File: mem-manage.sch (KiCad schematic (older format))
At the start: 15 parts, among them J2 Close to enable CAS latch, J3 Close to enable CAS latch, U11 8721, U3 74LS138, U31 74LS00, U54 74LS32, U61 74LS08, U7 8722, U9 74F32

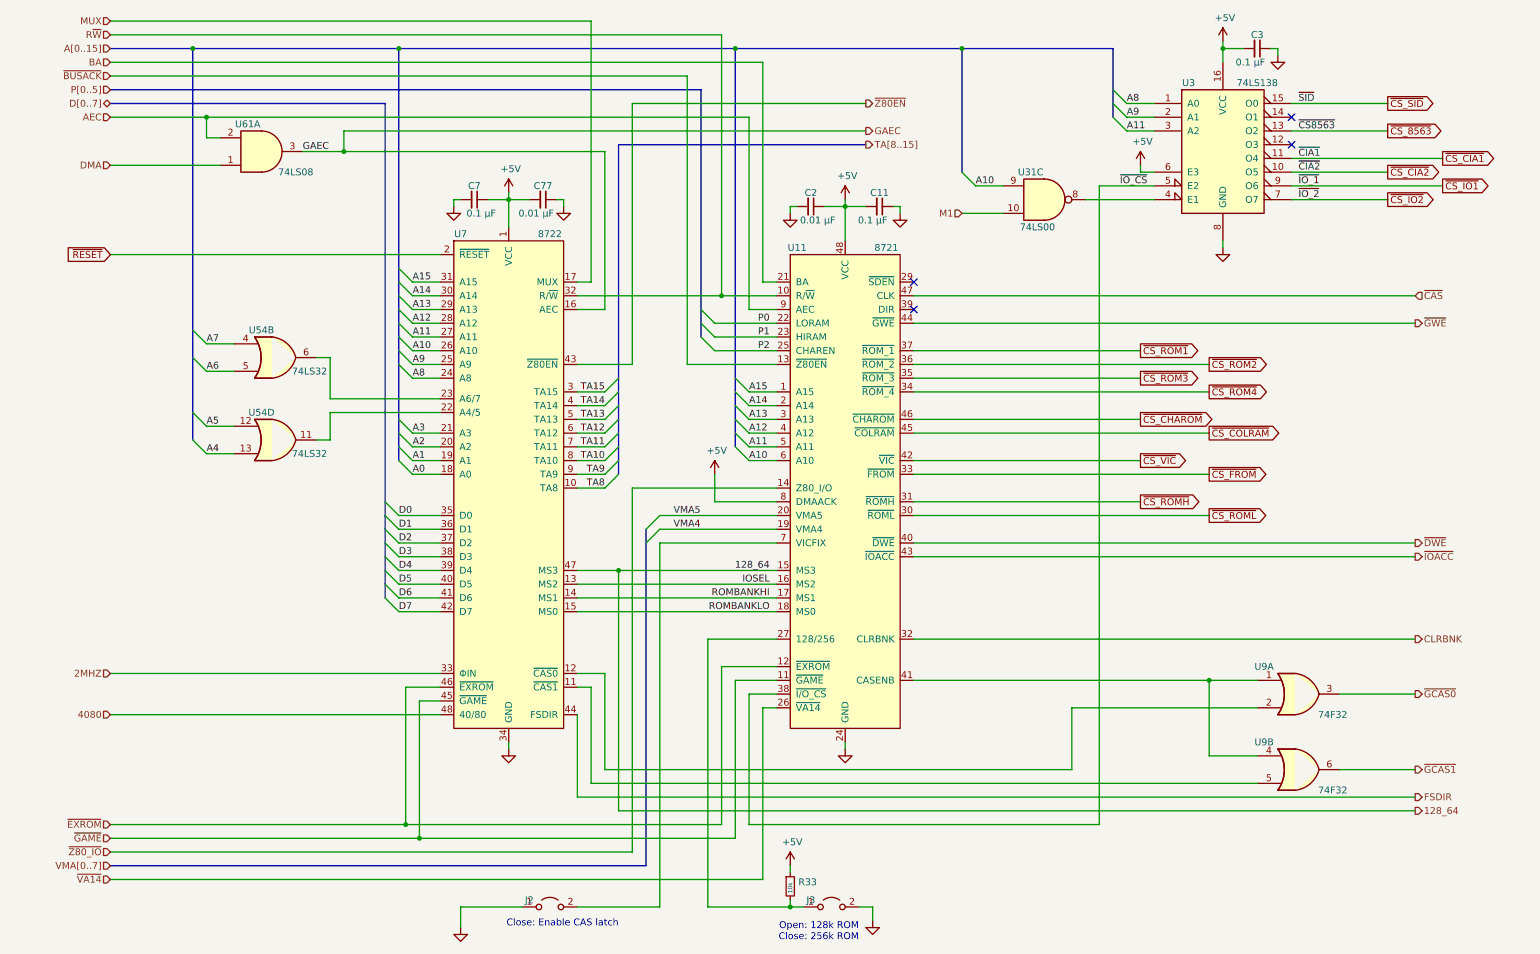
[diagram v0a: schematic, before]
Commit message: Clean up schematic
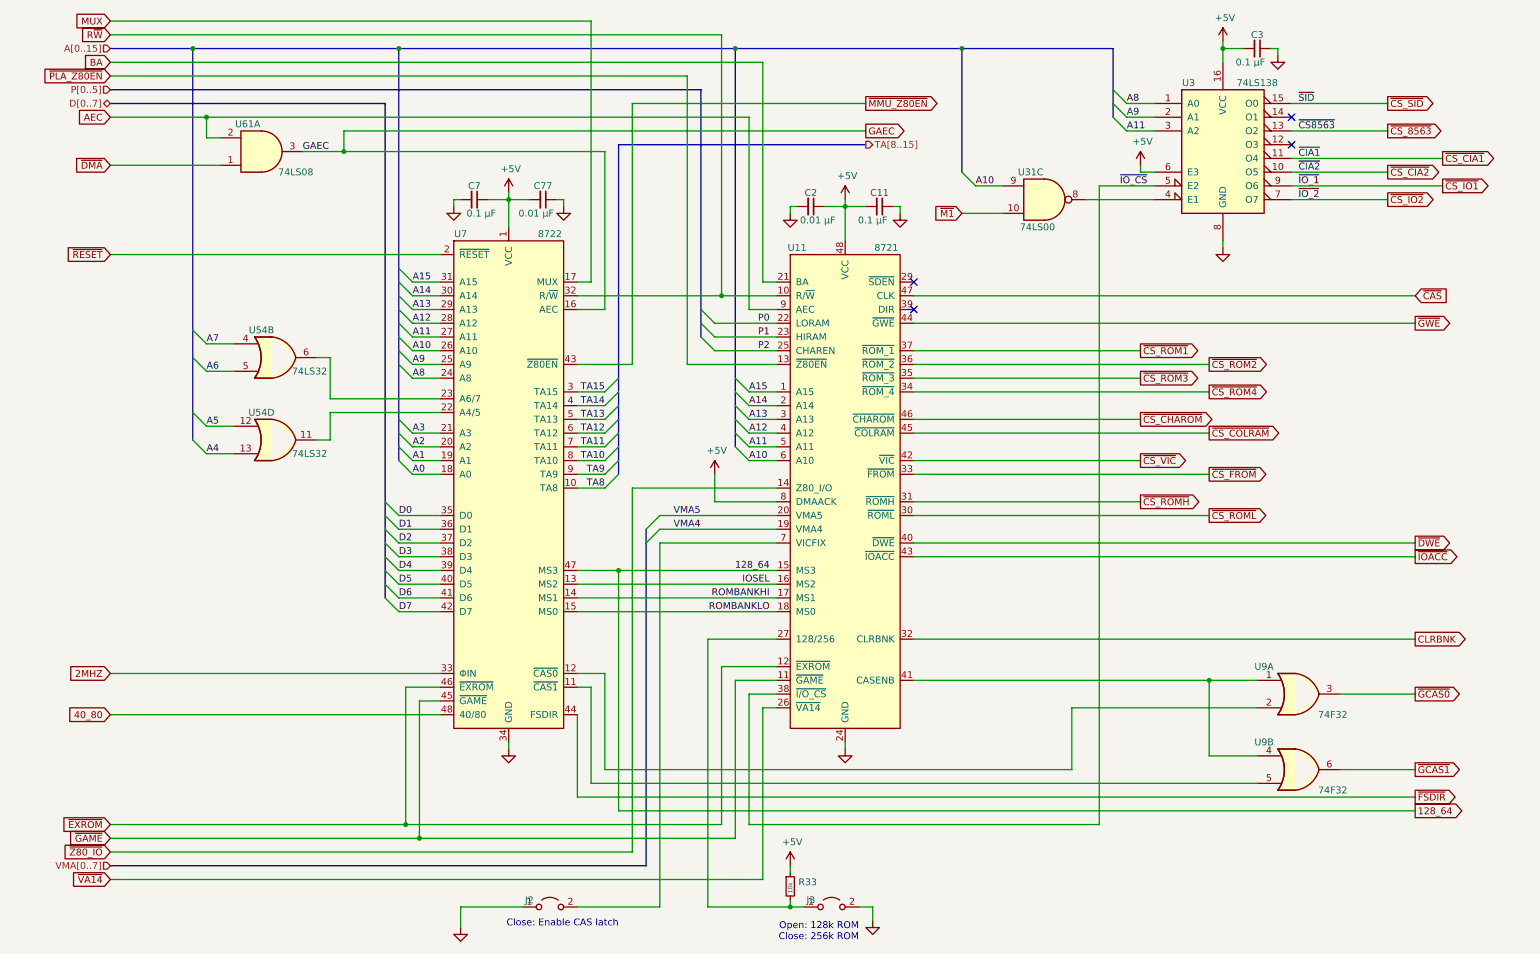
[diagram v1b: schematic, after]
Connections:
- net 4080 renamed 40_80
- net DMA renamed ~DMA
- net FSDIR renamed ~FSDIR
- net M1 renamed ~M1
- net ~BUSACK renamed ~PLA_Z80EN
- net ~Z80EN renamed ~MMU_Z80EN
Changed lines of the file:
@@
 Text HLabel 1000 1150 0    50   BiDi ~ 0
 D[0..7]
-Text HLabel 1000 5300 0    50   Input ~ 0
-2MHZ
 Wire Wire Line
 	1000 5300 3400 5300
-Text HLabel 1000 5600 0    50   Input ~ 0
-4080
 Wire Wire Line
 	1000 5600 3400 5600
@@
 Wire Wire Line
 	9950 6000 10500 6000
-Text HLabel 10500 6000 2    50   Output ~ 0
-~GCAS1
-Text HLabel 10500 5450 2    50   Output ~ 0
-~GCAS0
-Text HLabel 1000 6400 0    50   Input ~ 0
-~EXROM
-Text HLabel 1000 6500 0    50   Input ~ 0
-~GAME
 Wire Wire Line
 	1000 6400 3150 6400
@@
 Wire Wire Line
 	4700 4550 5850 4550
-Text HLabel 10500 6300 2    50   Output ~ 0
-128_64
 $Comp
 L Device:C_Small C7
@@
 	5450 2550 4400 2550
 Connection ~ 5450 2550
-Text HLabel 1000 650  0    50   Input ~ 0
-R~W
-Text HLabel 1000 550  0    50   Input ~ 0
-MUX
 Wire Wire Line
 	1000 550  4500 550
@@
 Wire Wire Line
 	1800 1600 1000 1600
-Text HLabel 1000 1600 0    50   Input ~ 0
-DMA
 Wire Wire Line
 	4600 1500 4600 2650
@@
 Text Label 2400 1500 0    50   ~ 0
 GAEC
-Text HLabel 1000 1250 0    50   Input ~ 0
-AEC
 Wire Wire Line
 	1000 1250 1700 1250
@@
 Wire Wire Line
 	1700 1250 5650 1250
-Text HLabel 6500 1350 2    50   Output ~ 0
-GAEC
-Text HLabel 6500 1150 2    50   Output ~ 0
-~Z80EN
 Wire Wire Line
 	4800 1150 4800 3050
@@
 Wire Wire Line
 	4800 1150 6500 1150
-Text HLabel 1000 950  0    50   Input ~ 0
-~BUSACK
 Wire Wire Line
 	1000 950  5200 950
@@
 Wire Wire Line
 	2700 1500 4600 1500
-Text HLabel 1000 850  0    50   Input ~ 0
-BA
 Wire Wire Line
 	1000 850  5750 850
@@
 Wire Wire Line
 	5750 2450 5850 2450
-Text HLabel 1000 6600 0    50   Input ~ 0
-~Z80_IO
 Wire Wire Line
 	1000 6600 4800 6600
@@
 Wire Wire Line
 	4400 6200 10500 6200
-Text HLabel 10500 6200 2    50   Output ~ 0
-FSDIR
 $Comp
 L power:+5V #PWR0298
@@
 Wire Wire Line
 	5750 6800 1000 6800
-Text HLabel 1000 6800 0    50   Input ~ 0
-~VA14
 $Comp
 L 74xx:74LS138 U3
@@
 Wire Bus Line
 	7200 750  8300 750
-Text HLabel 7200 1950 0    50   Input ~ 0
-M1
 Wire Wire Line
 	7200 1950 7500 1950
@@
 Wire Wire Line
 	6850 5050 10500 5050
-Text HLabel 10500 2550 2    50   Input ~ 0
-~CAS
-Text HLabel 10500 2750 2    50   Output ~ 0
-~GWE
-Text HLabel 10500 4350 2    50   Output ~ 0
-~DWE
-Text HLabel 10500 4450 2    50   Output ~ 0
-~IOACC
-Text HLabel 10500 5050 2    50   Output ~ 0
-CLRBNK
 $Comp
 L power:GND #PWR0304
@@
 Wire Bus Line
 	3100 750  3100 3750
+Text GLabel 1000 850  0    50   Input ~ 0
+BA
+Text GLabel 1000 650  0    50   Input ~ 0
+R~W
+Text GLabel 1000 1250 0    50   Input ~ 0
+AEC
+Text GLabel 10500 6200 2    50   Output ~ 0
+~FSDIR
+Text GLabel 10500 5050 2    50   Output ~ 0
+CLRBNK
+Text GLabel 1000 1600 0    50   Input ~ 0
+~DMA
+Text GLabel 1000 5300 0    50   Input ~ 0
+2MHZ
+Text GLabel 1000 550  0    50   Input ~ 0
+MUX
+Text GLabel 10500 2550 2    50   Input ~ 0
+~CAS
+Text GLabel 10500 2750 2    50   Output ~ 0
+~GWE
+Text GLabel 10500 4450 2    50   Output ~ 0
+~IOACC
+Text GLabel 10500 4350 2    50   Output ~ 0
+~DWE
+Text GLabel 1000 6800 0    50   Input ~ 0
+~VA14
+Text GLabel 1000 6400 0    50   Input ~ 0
+~EXROM
+Text GLabel 1000 6500 0    50   Input ~ 0
+~GAME
+Text GLabel 1000 6600 0    50   Input ~ 0
+~Z80_IO
+Text GLabel 10500 6300 2    50   Output ~ 0
+128_64
+Text GLabel 1000 950  0    50   Input ~ 0
+~PLA_Z80EN
+Text GLabel 6500 1350 2    50   Output ~ 0
+GAEC
+Text GLabel 6500 1150 2    50   Output ~ 0
+~MMU_Z80EN
+Text GLabel 7200 1950 0    50   Input ~ 0
+~M1
+Text GLabel 1000 5600 0    50   Input ~ 0
+40_80
+Text GLabel 10500 5450 2    50   Output ~ 0
+~GCAS0
+Text GLabel 10500 6000 2    50   Output ~ 0
+~GCAS1
 $EndSCHEMATC
